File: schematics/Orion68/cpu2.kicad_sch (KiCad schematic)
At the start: 39 parts, among them J10 Conn_02x08_Counter_Clockwise, J600 Euro96pin, J601 clock, J602 clock1, Q7 2N3904, Q8 2N3904, SW3 Reset, U16 74LS139, U2.? ICM7555xB, U21 74LS20, U22 74HC164, U24 74HC4078, U600 68000D, U601 74LS393, U602 74HC74, U603 74HC14, U604 ATmega8-16P

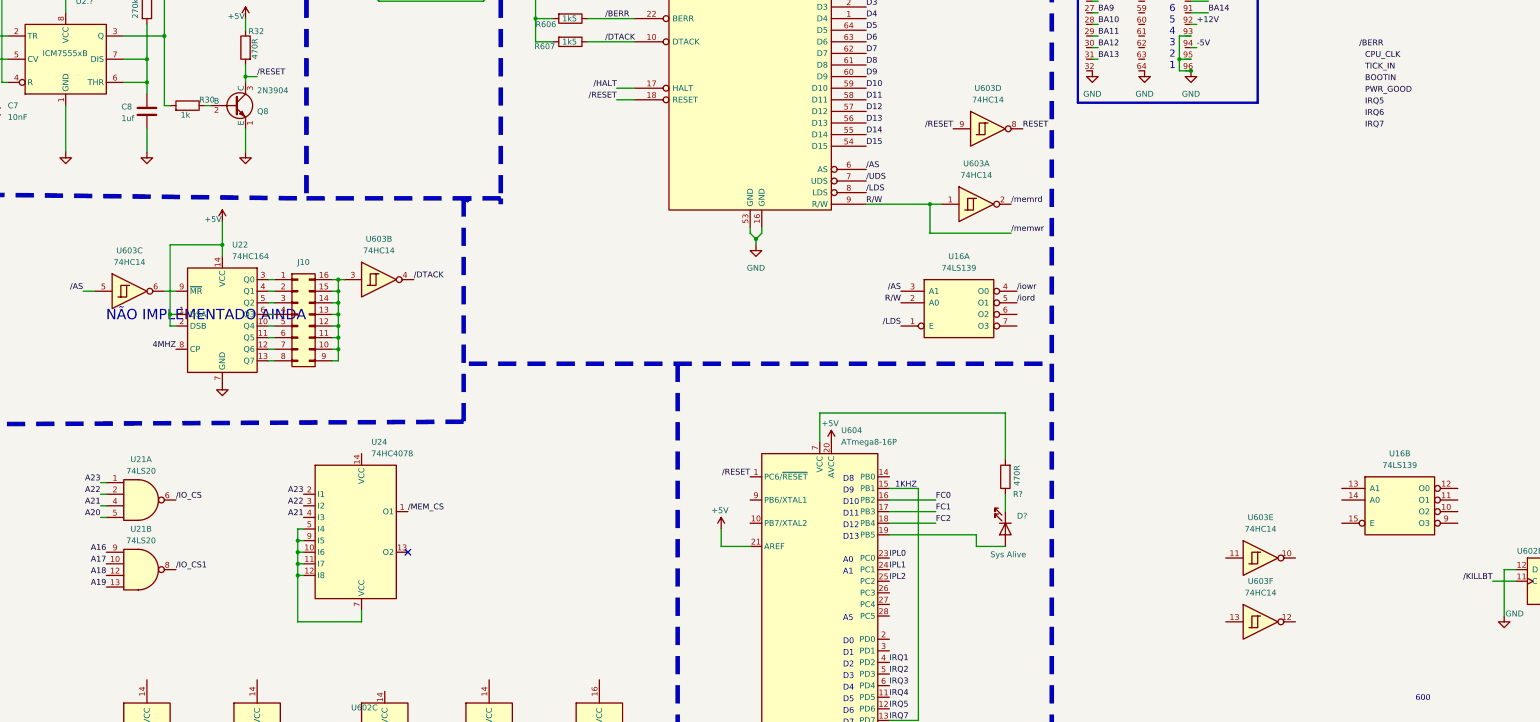
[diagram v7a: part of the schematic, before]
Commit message: Implemented VPA answer for interrupt running ok...18 20:12
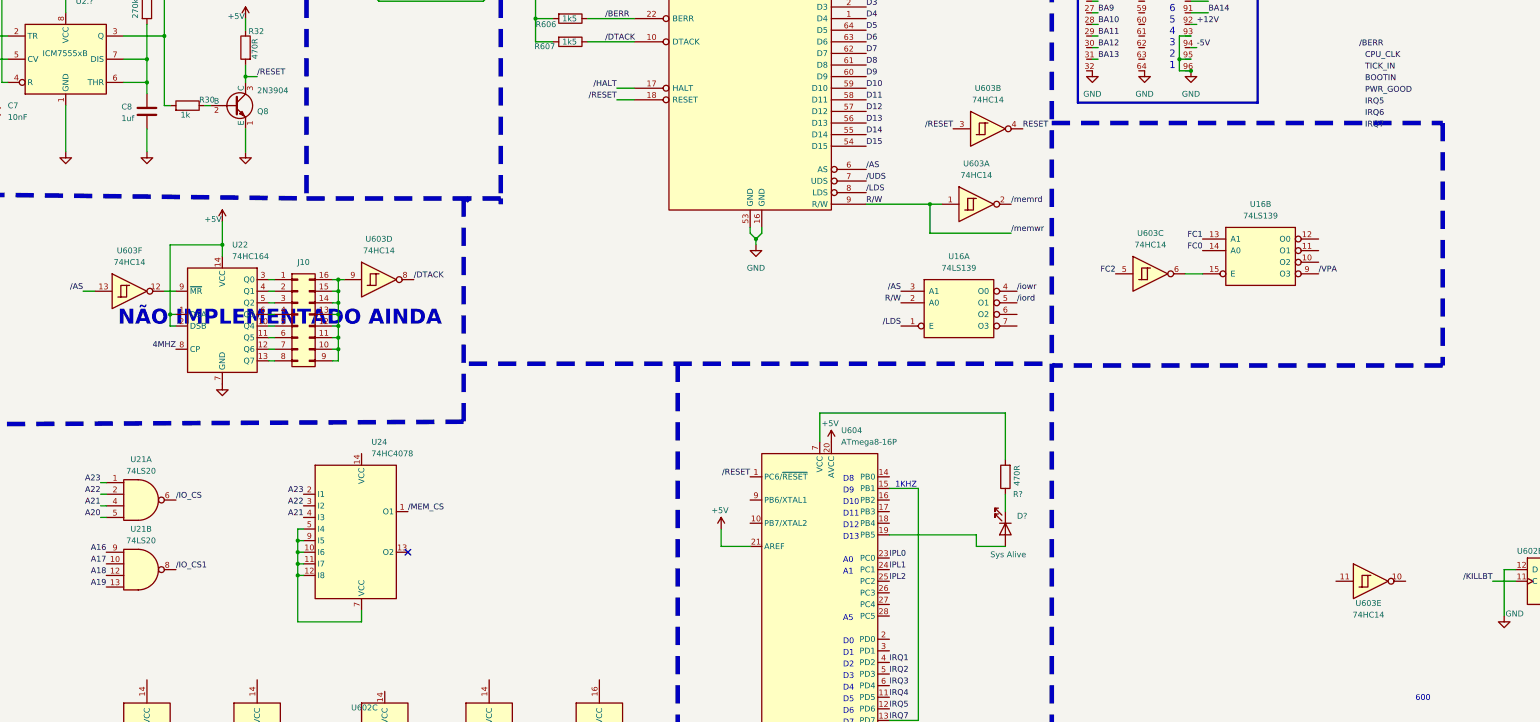
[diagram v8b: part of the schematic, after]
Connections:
- net FC0: now also U16.14 (A0); no longer U604.16 (PB2)
- net FC1: now also U16.13 (A1); no longer U604.17 (PB3)
- net FC2: now also U603.5; no longer U604.18 (PB4)
- net RESET: now also U603.4; no longer U603.8
- net /AS: now also U603.13; no longer U603.5
- net /DTACK: now also U603.8; no longer U603.4
- net /RESET: now also U603.3; no longer U603.9
- net /VPA: now also U16.9 (O3)
- net at U603.12: now also U22.9 (~{MR})
- net at U603.6: now also U16.15 (E); no longer U22.9 (~{MR})
- net at J10.10 (Pin_10), J10.11 (Pin_11), J10.12 (Pin_12)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: now also U603.9; no longer U603.3
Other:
- moved on the sheet: U16B, U603B, U603C, U603D, U603E, U603F
